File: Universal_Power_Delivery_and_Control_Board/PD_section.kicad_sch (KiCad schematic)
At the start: 49 parts, among them Q1 AO4407A, Q2 AO4407A, Q3 AO3401A, U1 CH224Q_C46061833, U2 TPS54202DDC, U3 USBLC6-2SC6, U4 USBLC6-2SC6, U5 ESD2CAN24-ES, U6 S2B-ZR (LF)(SN), U7 TPS259470LRPWR

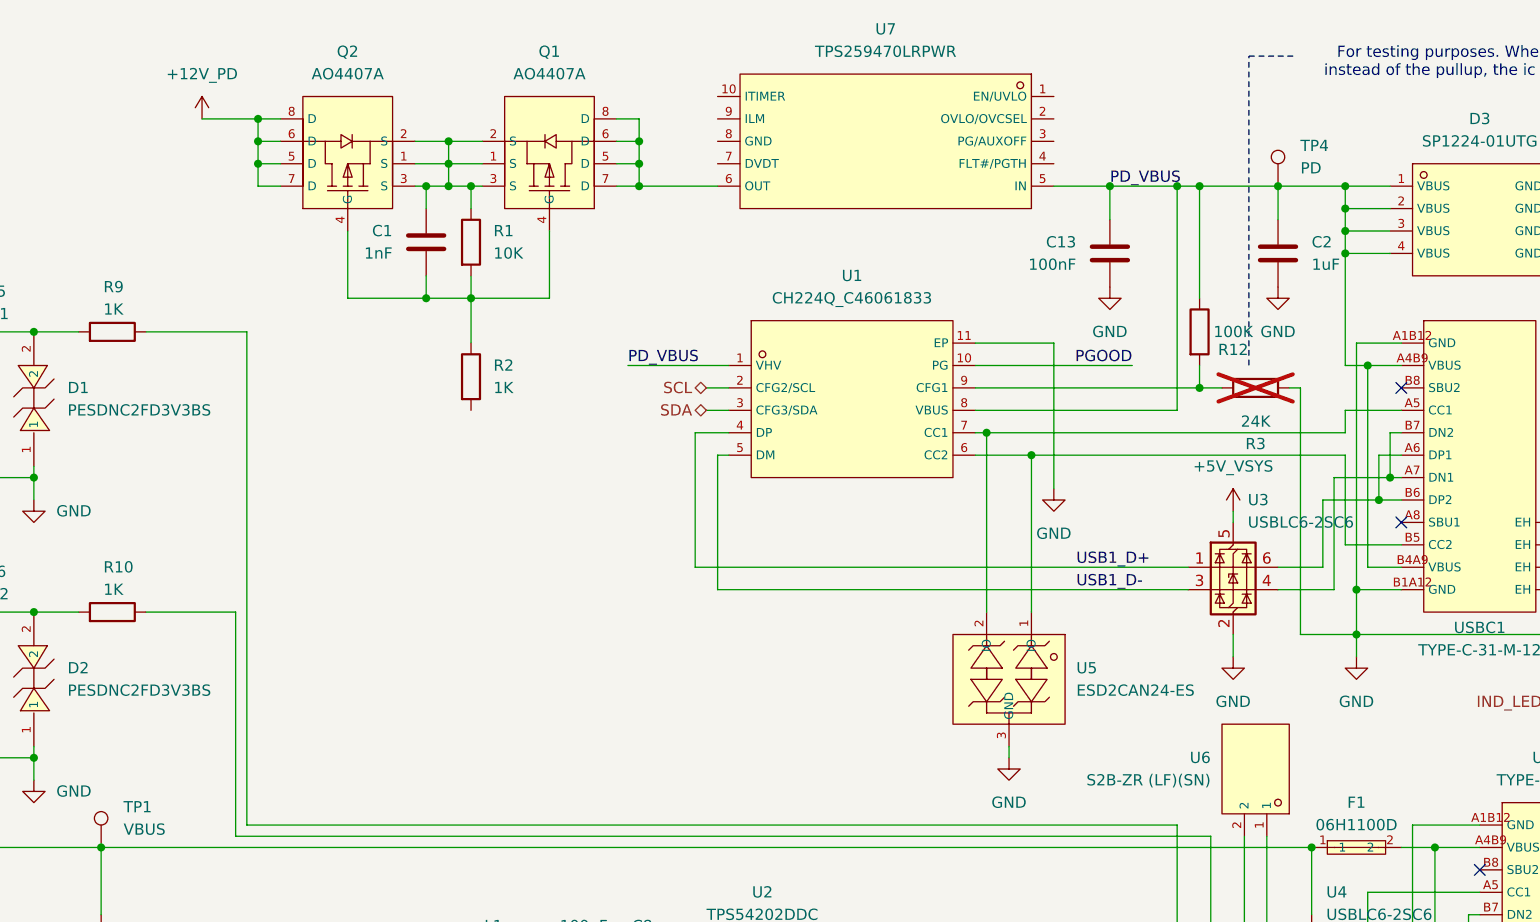
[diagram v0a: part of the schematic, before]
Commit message: Continued with routing on the UPDC and minor changes on the matrix board.
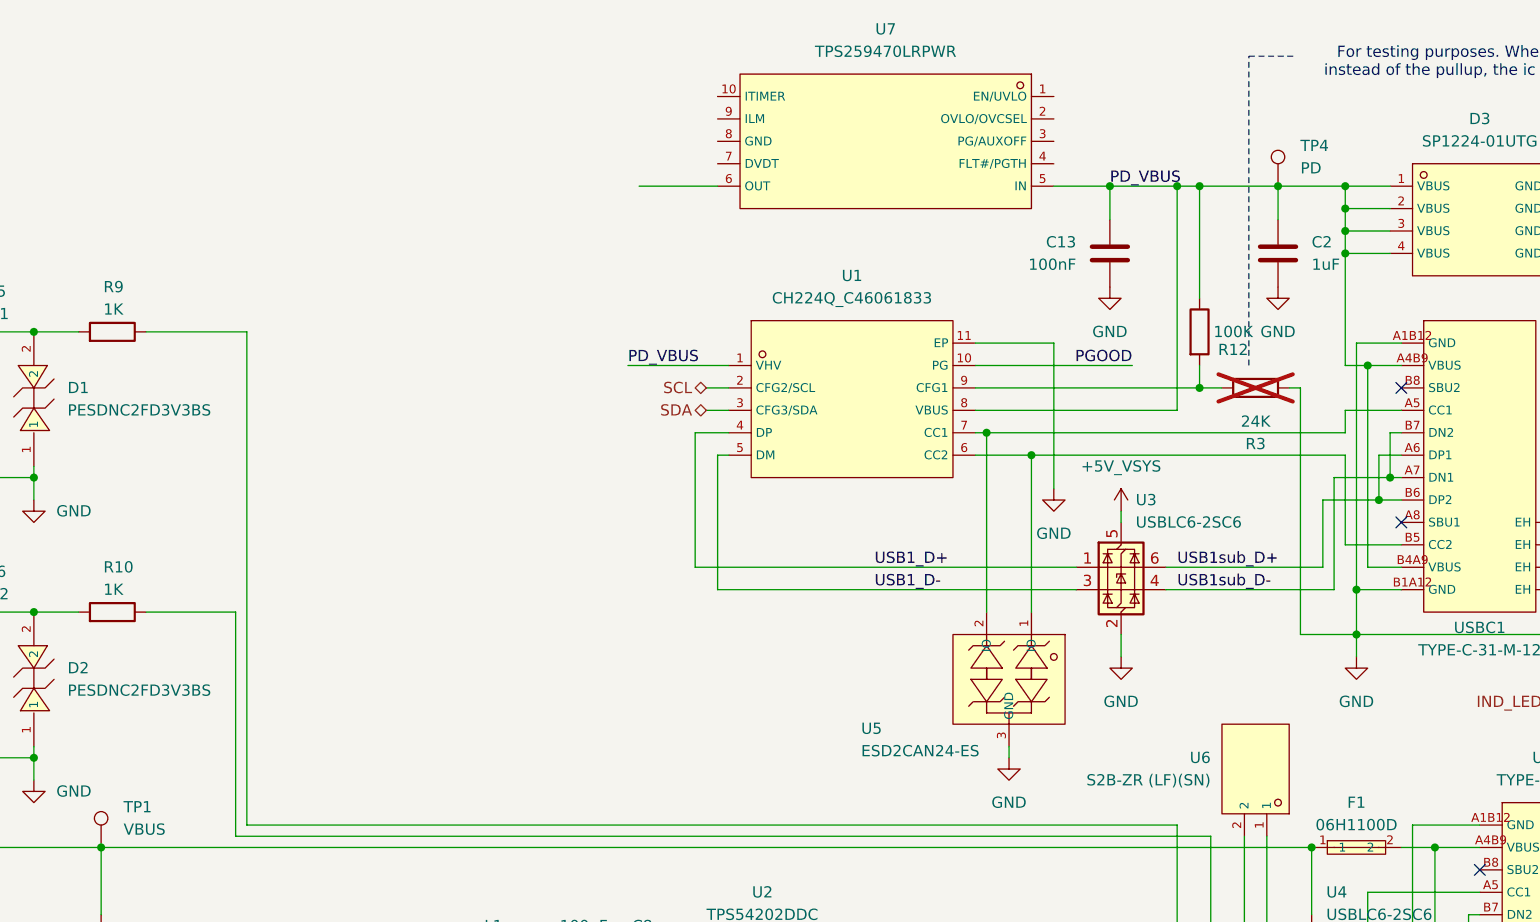
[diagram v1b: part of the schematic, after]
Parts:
- removed C1: 1nF, Capacitor_SMD:C_0402_1005Metric_Pad0.74x0.62mm_HandSolder, symbol Device:C
- removed Q1, Q2: AO4407A, lcsc_footprints:C16072_SOIC-8_L4_9-W3_9-P1_27-LS6_0-BL, symbol lcsc_imported:AO4407A
- removed R1: 10K, Resistor_SMD:R_0402_1005Metric_Pad0.72x0.64mm_HandSolder, symbol Device:R
- removed R2: 1K, Resistor_SMD:R_0402_1005Metric_Pad0.72x0.64mm_HandSolder, symbol Device:R
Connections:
- net USB1sub_D+: now reaches U3.6 (I/O1), USBC1.A6 (DP1), USBC1.B6 (DP2)
- net USB1sub_D-: now reaches U3.4 (I/O2), USBC1.A7 (DN1), USBC1.B7 (DN2)
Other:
- moved on the sheet: U3

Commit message: Imported the buck converter design block and contnued with the layout.
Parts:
- removed R12: 100K, Resistor_SMD:R_0402_1005Metric_Pad0.72x0.64mm_HandSolder, symbol Device:R
- added C24: 100uF, lcsc_footprints:C19673858_CAP-SMD_BD6_3-L6_5-W6_5-LS7_2-FD_1, symbol lcsc_imported:RZE-35V101MF80UQ-R2
- added C25, C26: ?, Capacitor_SMD:C_0402_1005Metric_Pad0.74x0.62mm_HandSolder, symbol Device:C
- added R15: 13.3K, Resistor_SMD:R_0402_1005Metric_Pad0.72x0.64mm_HandSolder, symbol Device:R
- R5: renamed from R3; now fitted
- renumbered C4 to C10, C3 to C11, C6 to C12, C7 to C13, C13 to C2, C2 to C3, C9 to C4, C11 to C5, C10 to C6, C12 to C7, C5 to C9, D3 to D1, D1 to D2, D2 to D3, Q3 to Q2, R5 to R10, R8 to R11, R9 to R3, R10 to R6, R11 to R7, R7 to R8, R6 to R9, TP4 to TP1, TP5 to TP2, TP6 to TP3, TP1 to TP4, TP3 to TP5, TP2 to TP6, U7 to U1, U1 to U2, U5 to U4, U6 to U5, U4 to U6, U2 to U7
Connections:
- net GND: now also U1.8 (GND), C24.2, C25.2, C26.2
- net at U1.10 (ITIMER): now also C26.1
- net PG_eFUSE: now reaches U1.3 (PG/AUXOFF)
- net +12V_PD: now reaches U1.6 (OUT)
- net +12V_PD: now also C24.1
- net at U1.7 (DVDT): now also C25.1
- net at U1.9 (ILM): now also R15.1
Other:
- note added: "Do not populate if the fastest overcurrent limiting behavior is desired."
- note added: "When this resistor is fitted, the ic defaults into 12V mode."
- note removed: "For testing purposes. When this resistor is fitted, instead of the pullup, the ic defaults into 12V mode."

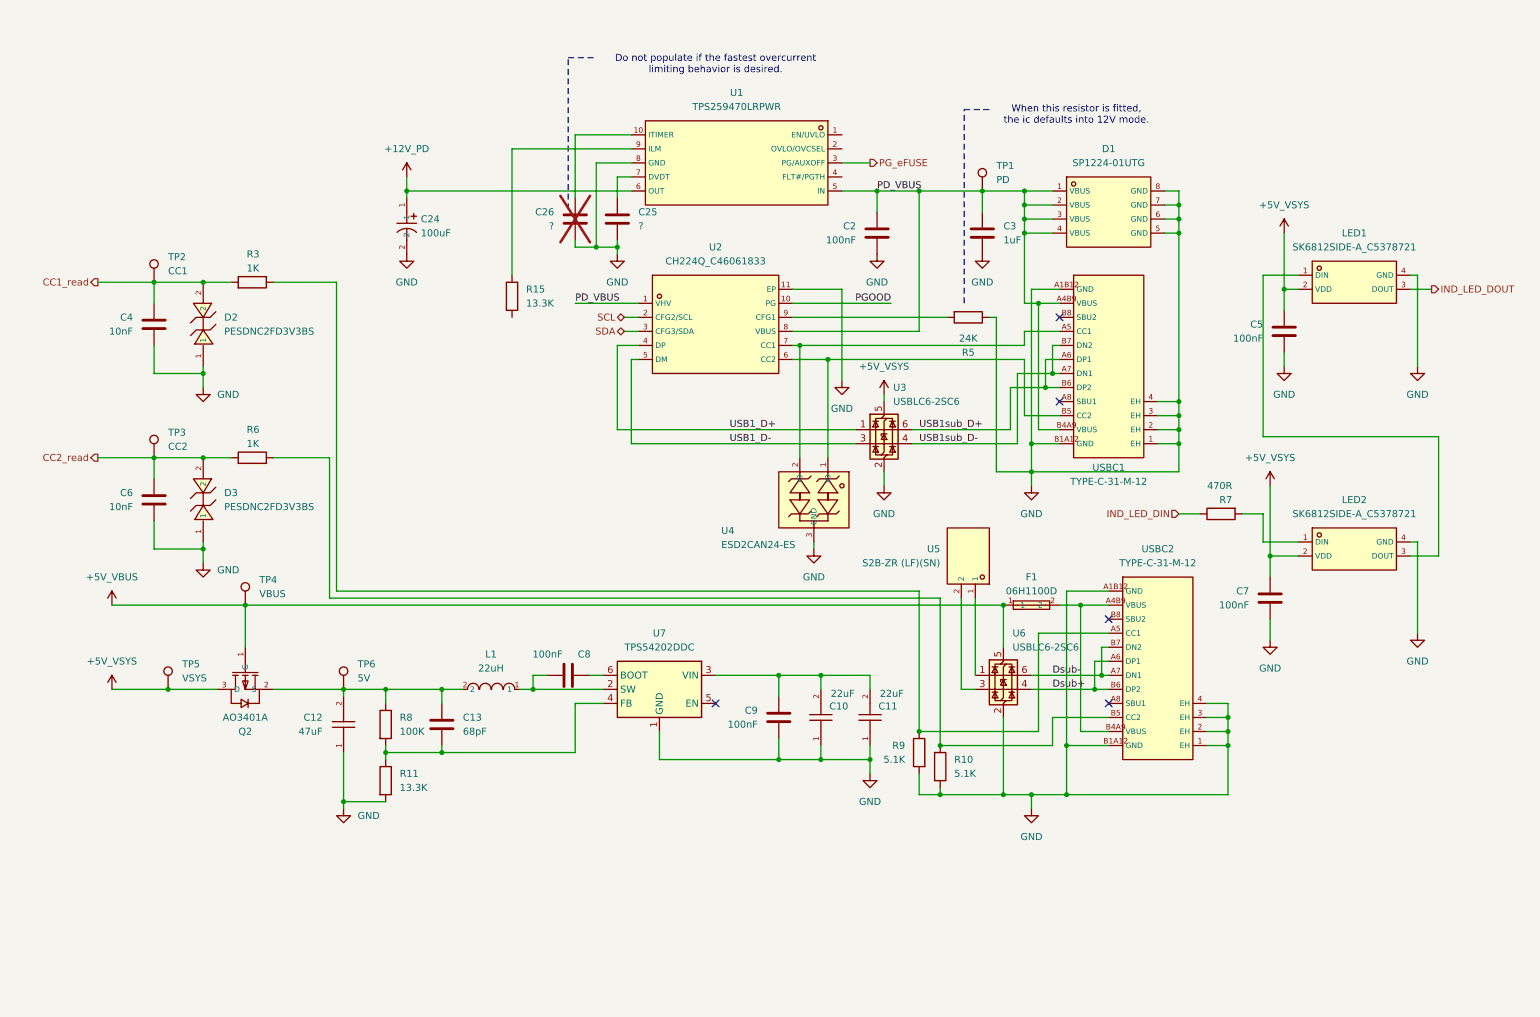
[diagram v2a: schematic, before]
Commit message: Restructured the schematic, added the digital output section and continued with the layout.
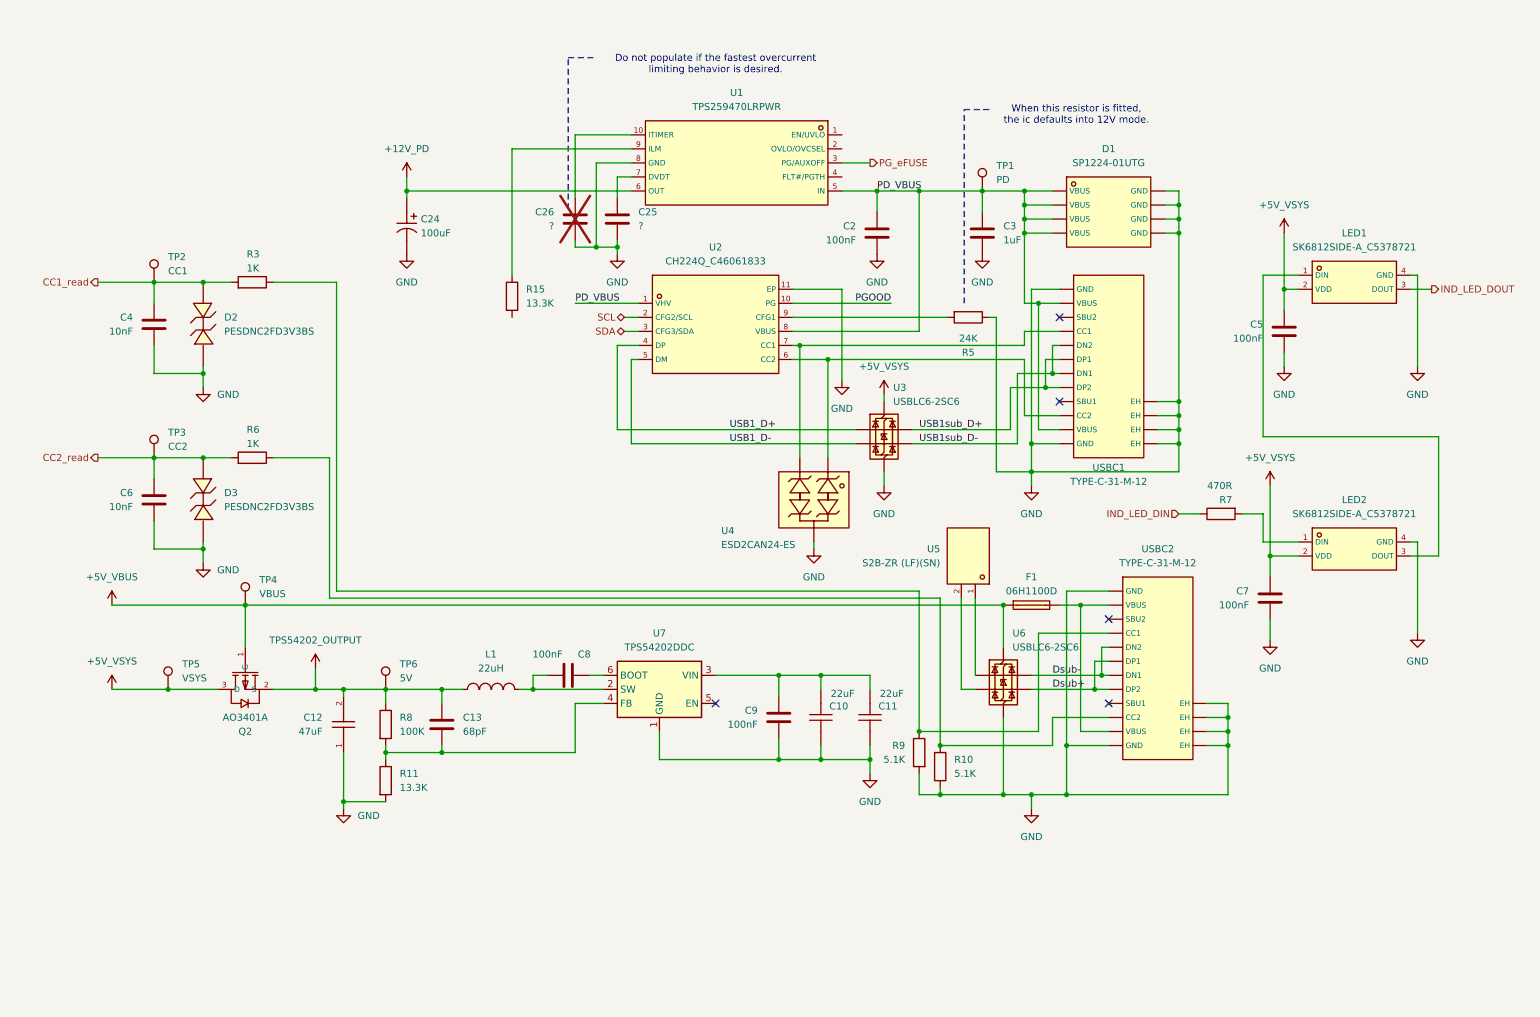
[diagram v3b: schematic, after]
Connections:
- net TPS54202_OUTPUT: now reaches C12.2, C13.1, L1.2, Q2.2 (S), R8.1, TP6.1
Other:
- moved on the sheet: TP6
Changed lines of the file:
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@@
 	)
 	(junction
+		(at 66.04 134.62)
+		(diameter 0)
+		(color 0 0 0 0)
+	)
+	(junction
 		(at 198.12 80.01)
 		(diameter 0)
@@
 	(wire
 		(pts
+			(xy 66.04 130.81) (xy 66.04 134.62)
+		)
+		(stroke
+			(width 0)
+			(type default)
+		)
+	)
+	(wire
+		(pts
 			(xy 195.58 95.25) (xy 195.58 90.17)
 		)
@@
 	(wire
 		(pts
+			(xy 58.42 134.62) (xy 66.04 134.62)
+		)
+		(stroke
+			(width 0)
+			(type default)
+		)
+	)
+	(wire
+		(pts
 			(xy 175.26 153.67) (xy 179.07 153.67)
 		)
@@
 	(wire
 		(pts
-			(xy 204.47 119.38) (xy 204.47 142.24)
+			(xy 66.04 134.62) (xy 71.12 134.62)
 		)
 		(stroke
@@
 	(wire
 		(pts
-			(xy 199.39 77.47) (xy 200.66 77.47)
+			(xy 204.47 119.38) (xy 204.47 142.24)
 		)
 		(stroke
@@
 	(wire
 		(pts
-			(xy 187.96 67.31) (xy 189.23 67.31)
+			(xy 199.39 77.47) (xy 200.66 77.47)
 		)
 		(stroke
@@
 	(wire
 		(pts
-			(xy 175.26 142.24) (xy 196.85 142.24)
+			(xy 187.96 67.31) (xy 189.23 67.31)
 		)
 		(stroke
@@
 	(wire
 		(pts
-			(xy 36.83 92.71) (xy 45.72 92.71)
+			(xy 175.26 142.24) (xy 196.85 142.24)
 		)
 		(stroke
@@
 	(wire
 		(pts
-			(xy 152.4 64.77) (xy 170.18 64.77)
+			(xy 36.83 92.71) (xy 45.72 92.71)
 		)
 		(stroke
@@
 	(wire
 		(pts
-			(xy 116.84 54.61) (xy 116.84 39.37)
+			(xy 152.4 64.77) (xy 170.18 64.77)
 		)
 		(stroke
@@
 	(wire
 		(pts
-			(xy 237.49 102.87) (xy 237.49 107.95)
+			(xy 116.84 54.61) (xy 116.84 39.37)
 		)
 		(stroke
@@
 	(wire
 		(pts
-			(xy 58.42 134.62) (xy 71.12 134.62)
+			(xy 237.49 102.87) (xy 237.49 107.95)
 		)
 		(stroke
@@
 	)
 	(symbol
+		(lib_name "PESDNC2FD3V3BS_1")
 		(lib_id "lcsc_imported:PESDNC2FD3V3BS")
 		(at 45.72 68.58 90)
@@
 	(symbol
 		(lib_id "Connector:TestPoint")
-		(at 71.12 134.62 0)
+		(at 78.74 134.62 0)
 		(unit 1)
 		(body_style 1)
@@
 		(fields_autoplaced yes)
 		(property "Reference" "TP6"
-			(at 73.66 130.0479 0)
+			(at 81.28 130.0479 0)
 			(show_name no)
 			(do_not_autoplace no)
@@
 		)
 		(property "Value" "5V"
-			(at 73.66 132.5879 0)
+			(at 81.28 132.5879 0)
 			(show_name no)
 			(do_not_autoplace no)
@@
 		)
 		(property "Footprint" "TestPoint:TestPoint_Pad_D1.0mm"
-			(at 76.2 134.62 0)
+			(at 83.82 134.62 0)
 			(hide yes)
 			(show_name no)
@@
 		)
 		(property "Datasheet" ""
-			(at 76.2 134.62 0)
+			(at 83.82 134.62 0)
 			(hide yes)
 			(show_name no)
@@
 		)
 		(property "Description" "test point"
-			(at 71.12 134.62 0)
+			(at 78.74 134.62 0)
 			(hide yes)
 			(show_name no)
@@
 	)
 	(symbol
+		(lib_name "GMK325BJ226MM-P_1")
 		(lib_id "lcsc_imported:GMK325BJ226MM-P")
 		(at 157.48 139.7 90)
@@
 	)
 	(symbol
+		(lib_name "TYPE-C-31-M-12_1")
 		(lib_id "lcsc_imported:TYPE-C-31-M-12")
 		(at 209.55 76.2 0)
@@
 	)
 	(symbol
+		(lib_name "USBLC6-2SC6_1")
 		(lib_id "Power_Protection:USBLC6-2SC6")
 		(at 190.5 132.08 0)
@@
 					(unit 1)
 				)
+			)
+		)
+	)
+	(symbol
+		(lib_id "power:+1V0")
+		(at 66.04 130.81 0)
+		(unit 1)
+		(body_style 1)
+		(exclude_from_sim no)
+		(in_bom yes)
+		(on_board yes)
+		(in_pos_files yes)
+		(dnp no)
+		(fields_autoplaced yes)
+		(property "Reference" "#PWR040"
+			(at 66.04 134.62 0)
+			(hide yes)
+			(show_name no)
+			(do_not_autoplace no)
+			(effects
+				(font
+					(size 1.27 1.27)
+				)
+			)
+		)
+		(property "Value" "TPS54202_OUTPUT"
+			(at 66.04 125.73 0)
+			(show_name no)
+			(do_not_autoplace no)
+			(effects
+				(font
+					(size 1.27 1.27)
+				)
+			)
+		)
+		(property "Footprint" ""
+			(at 66.04 130.81 0)
+			(hide yes)
+			(show_name no)
+			(do_not_autoplace no)
+			(effects
+				(font
+					(size 1.27 1.27)
+				)
+			)
+		)
+		(property "Datasheet" ""
+			(at 66.04 130.81 0)
+			(hide yes)
+			(show_name no)
+			(do_not_autoplace no)
+			(effects
+				(font
+					(size 1.27 1.27)
+				)
+			)
+		)
+		(property "Description" "Power symbol creates a global label with name \"+1V0\""
+			(at 66.04 130.81 0)
+			(hide yes)
+			(show_name no)
+			(do_not_autoplace no)
+			(effects
+				(font
+					(size 1.27 1.27)
+				)
+			)
+		)
+		(pin "1"
+		)
+		(instances
+			(project "Universal_Power_Delivery_and_Control_Board"
+				(path "/b749dd2f-6b66-411b-a989-65da6091f700/ecb712a9-952e-410c-aeaa-ac56dd2d7726"
+					(reference "#PWR040")
+					(unit 1)
+				)

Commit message: Switched to a 4 layer stackup and routed the digital output section.
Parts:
- removed C26: ?, Capacitor_SMD:C_0402_1005Metric_Pad0.74x0.62mm_HandSolder, symbol Device:C
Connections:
- no-connect marks 5 -> 6
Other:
- note removed: "Do not populate if the fastest overcurrent limiting behavior is desired."
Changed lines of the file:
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@@
 	(generator_version "10.0")
 	(paper "A4")
-	(text "Do not populate if the fastest overcurrent\nlimiting behavior is desired."
-		(exclude_from_sim no)
-		(at 138.43 21.59 0)
-		(effects
-			(font
-				(size 1.27 1.27)
-			)
-		)
-	)
 	(text "When this resistor is fitted,\nthe ic defaults into 12V mode.\n"
 		(exclude_from_sim no)
@@
 	)
 	(junction
-		(at 116.84 54.61)
-		(diameter 0)
-		(color 0 0 0 0)
-	)
-	(junction
 		(at 157.48 147.32)
 		(diameter 0)
@@
 		(at 209.55 137.16)
 	)
+	(no_connect
+		(at 123.19 34.29)
+	)
 	(wire
 		(pts
@@
 	(wire
 		(pts
-			(xy 113.03 34.29) (xy 113.03 45.72)
-		)
-		(stroke
-			(width 0)
-			(type default)
-		)
-	)
-	(wire
-		(pts
 			(xy 116.84 39.37) (xy 123.19 39.37)
 		)
@@
 	(wire
 		(pts
-			(xy 113.03 54.61) (xy 116.84 54.61)
-		)
-		(stroke
-			(width 0)
-			(type default)
-		)
-	)
-	(wire
-		(pts
 			(xy 175.26 44.45) (xy 175.26 69.85)
 		)
@@
 	(wire
 		(pts
-			(xy 113.03 53.34) (xy 113.03 54.61)
-		)
-		(stroke
-			(width 0)
-			(type default)
-		)
-	)
-	(wire
-		(pts
 			(xy 200.66 72.39) (xy 199.39 72.39)
 		)
@@
 		)
 	)
-	(polyline
-		(pts
-			(xy 111.76 20.32) (xy 116.84 20.32)
-		)
-		(stroke
-			(width 0)
-			(type dash_dot_dot)
-			(color 255 105 0 1)
-		)
-	)
 	(wire
 		(pts
@@
 	(wire
 		(pts
-			(xy 113.03 34.29) (xy 123.19 34.29)
-		)
-		(stroke
-			(width 0)
-			(type default)
-		)
-	)
-	(wire
-		(pts
 			(xy 194.31 44.45) (xy 199.39 44.45)
 		)
@@
 		)
 	)
-	(polyline
-		(pts
-			(xy 111.76 47.752) (xy 111.76 20.32)
-		)
-		(stroke
-			(width 0)
-			(type dash_dot_dot)
-			(color 255 105 0 1)
-		)
-	)
 	(wire
 		(pts
@@
 					(unit 1)
 				)
-			)
-		)
-	)
-	(symbol
-		(lib_id "Device:C")
-		(at 113.03 49.53 0)
-		(unit 1)
-		(body_style 1)
-		(exclude_from_sim no)
-		(in_bom yes)
-		(on_board yes)
-		(in_pos_files yes)
-		(dnp yes)
-		(property "Reference" "C26"
-			(at 109.22 48.2599 0)
-			(show_name no)
-			(do_not_autoplace no)
-			(effects
-				(font
-					(size 1.27 1.27)
-				)
-				(justify right)
-			)
-		)
-		(property "Value" "?"
-			(at 109.22 50.7999 0)
-			(show_name no)
-			(do_not_autoplace no)
-			(effects
-				(font
-					(size 1.27 1.27)
-				)
-				(justify right)
-			)
-		)
-		(property "Footprint" "Capacitor_SMD:C_0402_1005Metric_Pad0.74x0.62mm_HandSolder"
-			(at 113.9952 53.34 0)
-			(hide yes)
-			(show_name no)
-			(do_not_autoplace no)
-			(effects
-				(font
-					(size 1.27 1.27)
-				)
-			)
-		)
-		(property "Datasheet" ""
-			(at 113.03 49.53 0)
-			(hide yes)
-			(show_name no)
-			(do_not_autoplace no)
-			(effects
-				(font
-					(size 1.27 1.27)
-				)
-			)
-		)
-		(property "Description" "Unpolarized capacitor"
-			(at 113.03 49.53 0)
-			(hide yes)
-			(show_name no)
-			(do_not_autoplace no)
-			(effects
-				(font
-					(size 1.27 1.27)
-				)
-			)
-		)
-		(pin "1"
-		)
-		(pin "2"
-		)
-		(instances
-			(project "Universal_Power_Delivery_and_Control_Board"
-				(path "/b749dd2f-6b66-411b-a989-65da6091f700/ecb712a9-952e-410c-aeaa-ac56dd2d7726"
-					(reference "C26")
-					(unit 1)
-				)
